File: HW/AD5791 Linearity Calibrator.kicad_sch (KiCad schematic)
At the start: 56 parts, among them J1 OUTPUT, J10 Conn_01x01, J2 PWR, J3 REF, J4 REF, J5 REF, J6 REF, J7 Conn_01x01, J8 Conn_01x01, J9 Conn_01x01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

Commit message: Layout Rev 2 Finished?
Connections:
- net UART_RX: now reaches U12.6 (VOB)
- net UART_RX: now also U1.2 (GPIO1)
- net UART_TX: now reaches U12.7 (VIA)
- net UART_TX: now also U1.1 (GPIO0)
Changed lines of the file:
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@@
+    (stroke (width 0) (type default))
+  )
+  (wire (pts (xy 231.14 173.99) (xy 240.03 173.99))
     (stroke (width 0) (type default))
   )
@@
   )
   (wire (pts (xy 217.17 255.27) (xy 207.01 255.27))
+    (stroke (width 0) (type default))
+  )
+  (wire (pts (xy 231.14 179.07) (xy 240.03 179.07))
     (stroke (width 0) (type default))
   )
@@
     (effects (font (size 1.27 1.27)) (justify right bottom))
   )
+  (label "UART_RX" (at 316.23 167.64 0) (fields_autoplaced)
+    (effects (font (size 1.27 1.27)) (justify left bottom))
+  )
   (label "~{LDAC}" (at 226.06 92.71 0) (fields_autoplaced)
     (effects (font (size 1.27 1.27)) (justify left bottom))
@@
     (effects (font (size 1.27 1.27)) (justify left bottom))
   )
+  (label "UART_TX" (at 240.03 173.99 180) (fields_autoplaced)
+    (effects (font (size 1.27 1.27)) (justify right bottom))
+  )
   (label "REF" (at 74.93 129.54 180) (fields_autoplaced)
     (effects (font (size 1.27 1.27)) (justify right bottom))
@@
     (effects (font (size 1.27 1.27)) (justify left bottom))
   )
+  (label "UART_RX" (at 240.03 179.07 180) (fields_autoplaced)
+    (effects (font (size 1.27 1.27)) (justify right bottom))
+  )
+  (label "UART_TX" (at 316.23 165.1 0) (fields_autoplaced)
+    (effects (font (size 1.27 1.27)) (justify left bottom))
+  )

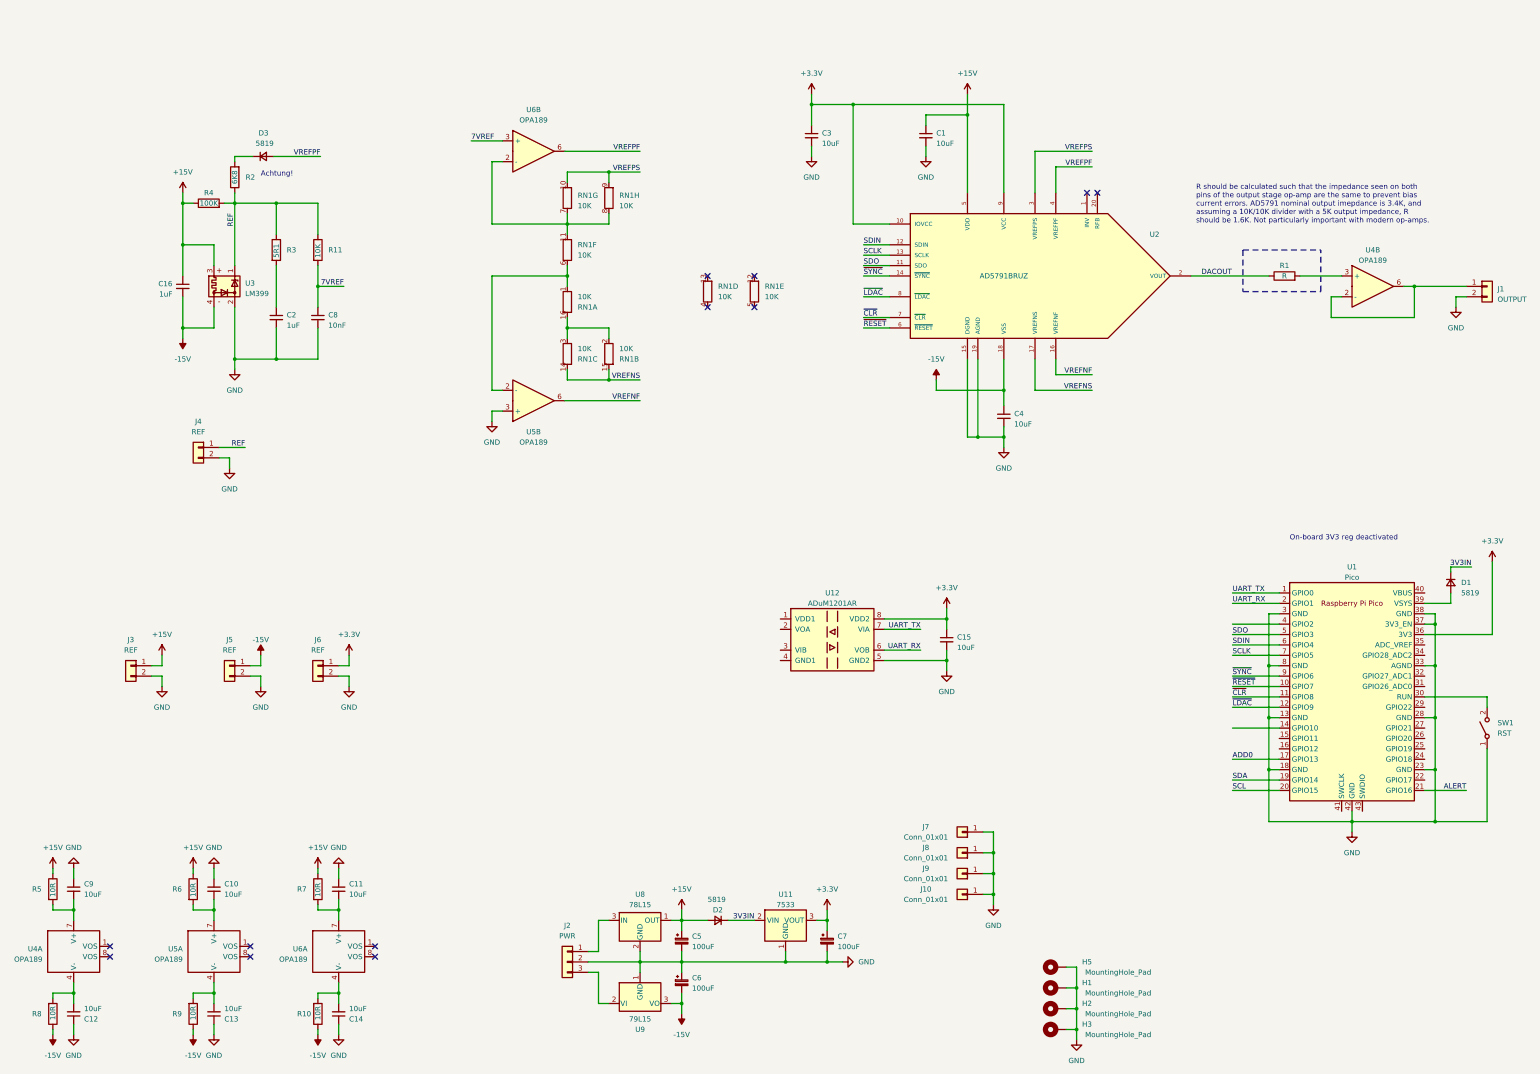
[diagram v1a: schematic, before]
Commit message: 4 wire buffer, keepout under isolator traces
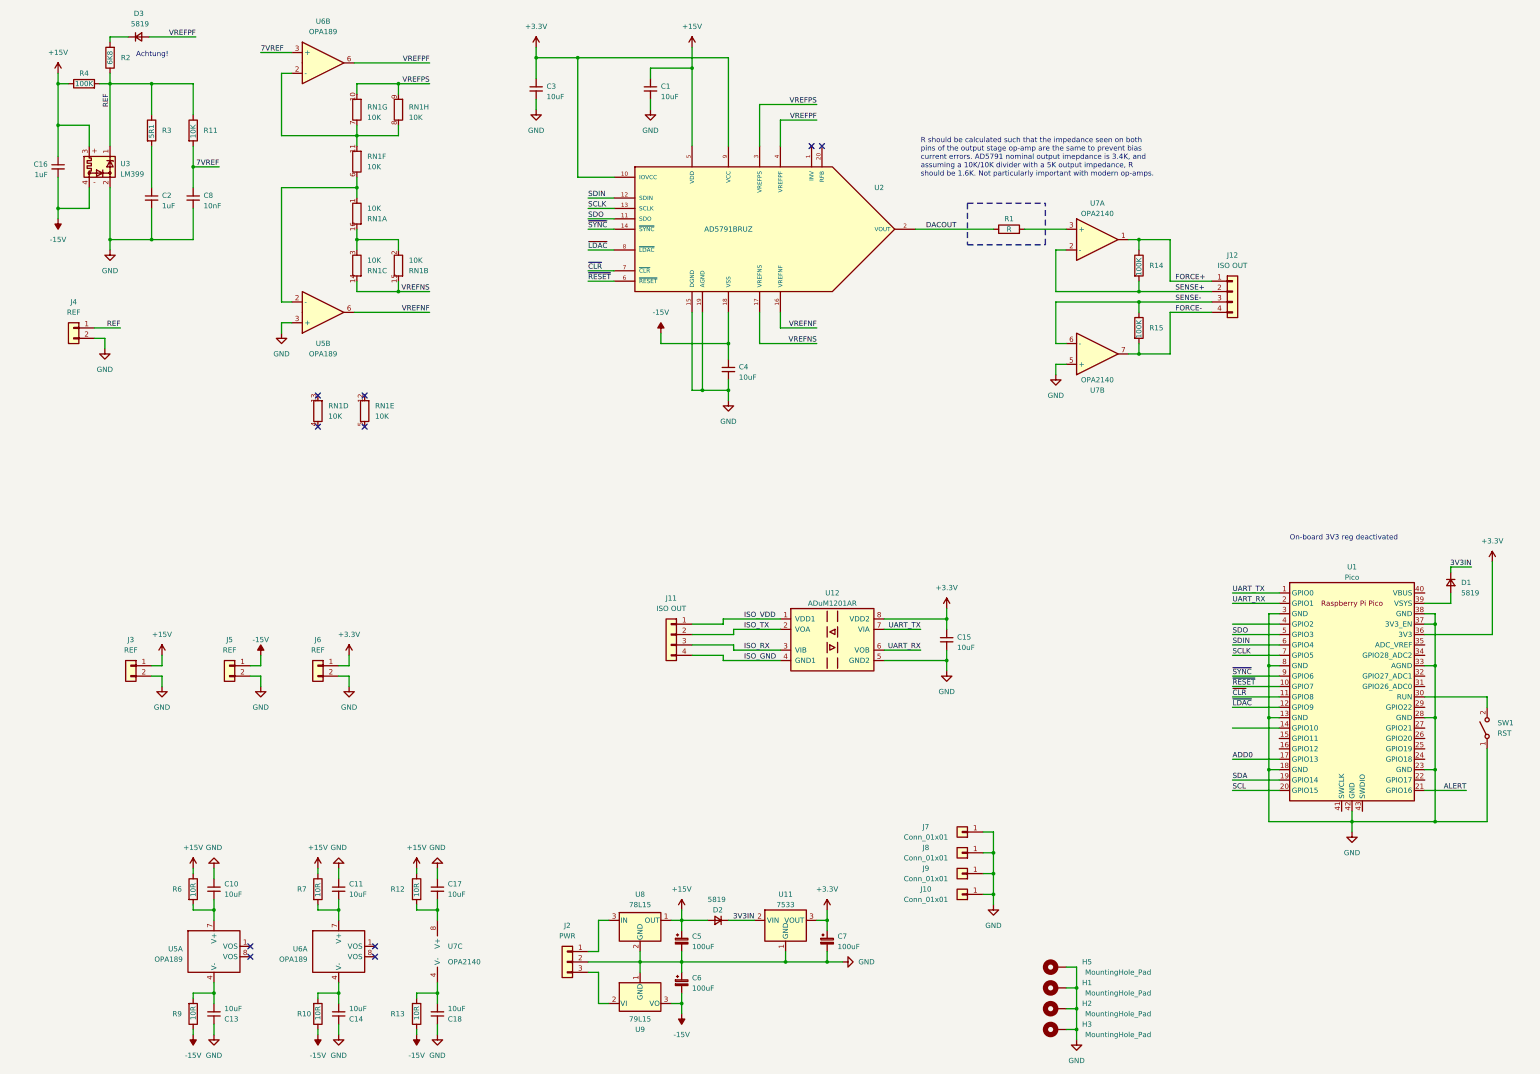
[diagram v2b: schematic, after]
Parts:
- removed C12, C9: 10uF, Resistor_SMD:R_0603_1608Metric, symbol Device:C_Small
- removed J1: OUTPUT, Connector_PinHeader_2.54mm:PinHeader_1x02_P2.54mm_Vertical, symbol Connector_Generic:Conn_01x02
- removed R5, R8: 10R, Resistor_SMD:R_0603_1608Metric, symbol Device:R
- removed U4: OPA189, Package_SO:SOIC-8_3.9x4.9mm_P1.27mm, symbol Better Op-Amp:Better_Op-Amp
- added C17, C18: 10uF, Resistor_SMD:R_0603_1608Metric, symbol Device:C_Small
- added J11, J12: ISO OUT, Connector_PinHeader_2.54mm:PinHeader_1x04_P2.54mm_Vertical, symbol Connector_Generic:Conn_01x04
- added R12, R13: 10R, Resistor_SMD:R_0603_1608Metric, symbol Device:R
- added R14, R15: 100K, Resistor_SMD:R_0603_1608Metric, symbol Device:R
- added U7: OPA2140, Package_SO:SOIC-8_3.9x4.9mm_P1.27mm, symbol Device:Opamp_Dual
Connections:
- net +15V: now also R12.1
- net -15V: now also R13.1
- net GND: now also C17.1, C18.1, U7.5 (+)
- net at R1.2: now also U7.3 (+)
- net ISO_VDD: now reaches U12.1 (VDD1)
- net ISO_VDD: now also J11.1 (Pin_1)
- net ISO_TX: now reaches U12.2 (VOA)
- net ISO_TX: now also J11.2 (Pin_2)
- net ISO_RX: now reaches U12.3 (VIB)
- net ISO_RX: now also J11.3 (Pin_3)
- net ISO_GND: now reaches U12.4 (GND1)
- net ISO_GND: now also J11.4 (Pin_4)
- new net: C17.2, R12.2, U7.8 (V+)
- new net: C18.2, R13.2, U7.4 (V-)
- new net FORCE+: J12.1 (Pin_1), R14.1, U7.1
- new net FORCE-: J12.4 (Pin_4), R15.2, U7.7
- new net SENSE+: J12.2 (Pin_2), R14.2, U7.2 (-)
- new net SENSE-: J12.3 (Pin_3), R15.1, U7.6 (-)
- no-connect marks 12 -> 10
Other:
- moved on the sheet: C1, C16, C2, C3, C4, C8, D3, J4, R1, R11, R2, R3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

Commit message: Layout Rev 3
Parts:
- added C9: 10uF, Resistor_SMD:R_0603_1608Metric, symbol Device:C_Small
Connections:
- net ISO_GND: now also C9.2
- net ISO_VDD: now also C9.1
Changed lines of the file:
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@@
+    (stroke (width 0) (type default))
+  )
+  (wire (pts (xy 260.35 170.18) (xy 260.35 173.99))
     (stroke (width 0) (type default))
   )
@@
     (stroke (width 0) (type default))
   )
+  (wire (pts (xy 260.35 179.07) (xy 260.35 184.15))
+    (stroke (width 0) (type default))
+  )
   (wire (pts (xy 62.23 264.16) (xy 62.23 262.89))
     (stroke (width 0) (type default))
@@
     (effects (font (size 1.27 1.27)) (justify left bottom))
   )
+  (label "ISO_GND" (at 260.35 184.15 0) (fields_autoplaced)
+    (effects (font (size 1.27 1.27)) (justify left bottom))
+  )
   (label "SDA" (at 316.23 210.82 0) (fields_autoplaced)
     (effects (font (size 1.27 1.27)) (justify left bottom))
   )
   (label "ISO_GND" (at 196.85 181.61 0) (fields_autoplaced)
+    (effects (font (size 1.27 1.27)) (justify left bottom))
+  )
+  (label "ISO_VDD" (at 260.35 170.18 0) (fields_autoplaced)
     (effects (font (size 1.27 1.27)) (justify left bottom))
   )
@@
         )
       )
+    )
+  )
+  (symbol (lib_id "Device:C_Small") (at 260.35 176.53 0) (unit 1)
+    (in_bom yes) (on_board yes) (dnp no) (fields_autoplaced)
+    (property "Reference" "C9" (at 262.89 175.9013 0)
+      (effects (font (size 1.27 1.27)) (justify left))
+    )
+    (property "Value" "10uF" (at 262.89 178.4413 0)
+      (effects (font (size 1.27 1.27)) (justify left))
+    )
+    (property "Footprint" "Resistor_SMD:R_0603_1608Metric" (at 260.35 176.53 0)
+      (effects (font (size 1.27 1.27)) hide)
+    )
+    (property "Datasheet" "~" (at 260.35 176.53 0)
+      (effects (font (size 1.27 1.27)) hide)
+    )
+    (pin "1")
+    (pin "2")
+    (instances
+      (project "AD5791 Linearity Calibrator"
+        (path "/545249ea-2c8e-4b30-8f2b-5f4518163292"
+          (reference "C9") (unit 1)
+        )
+      )

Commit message: star ground added
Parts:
- added JP1: GND BRIDGE, 0603 Jumper:0603 Jumper, symbol Jumper:SolderJumper_2_Open
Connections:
- net GND: now also JP1.1 (A); no longer C2.2, C8.2, U2.19 (AGND), U3.2, U5.3 (+), U7.5 (+)
- new net GNDA: C2.2, C8.2, JP1.2 (B), U2.19 (AGND), U3.2, U5.3 (+), U7.5 (+)

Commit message: Layout Rev 4
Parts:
- added D4: 5819, Resistor_SMD:R_0603_1608Metric_Pad0.98x0.95mm_HandSolder, symbol Device:D_Small
- R11: footprint Resistor_SMD:R_0603_1608Metric -> 0603 Jumper:0603 Jumper
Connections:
- net +15V: now also D4.1 (K)
- net +3.3V: now also D4.2 (A)
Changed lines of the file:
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@@
   (junction (at 146.05 34.29) (diameter 0) (color 0 0 0 0)
   )
+  (junction (at 193.04 53.34) (diameter 0) (color 0 0 0 0)
+  )
   (junction (at 193.04 115.57) (diameter 0) (color 0 0 0 0)
   )
@@
   (junction (at 278.13 266.7) (diameter 0) (color 0 0 0 0)
   )
+  (junction (at 184.15 53.34) (diameter 0) (color 0 0 0 0)
+  )
   (junction (at 246.38 171.45) (diameter 0) (color 0 0 0 0)
   )
@@
     (stroke (width 0) (type default))
   )
-  (wire (pts (xy 184.15 55.88) (xy 184.15 36.83))
+  (wire (pts (xy 184.15 55.88) (xy 184.15 53.34))
     (stroke (width 0) (type default))
   )
@@
     (stroke (width 0) (type default))
   )
+  (wire (pts (xy 184.15 53.34) (xy 184.15 36.83))
+    (stroke (width 0) (type default))
+  )
   (wire (pts (xy 293.37 88.9) (xy 293.37 91.44))
     (stroke (width 0) (type default))
@@
     (stroke (width 0) (type default))
   )
-  (wire (pts (xy 193.04 34.29) (xy 193.04 55.88))
+  (wire (pts (xy 193.04 34.29) (xy 193.04 53.34))
     (stroke (width 0) (type default))
   )
@@
     (stroke (width 0) (type default))
   )
+  (wire (pts (xy 190.5 53.34) (xy 193.04 53.34))
+    (stroke (width 0) (type default))
+  )
   (wire (pts (xy 316.23 205.74) (xy 327.66 205.74))
     (stroke (width 0) (type default))
@@
     (stroke (width 0) (type default))
   )
+  (wire (pts (xy 193.04 53.34) (xy 193.04 55.88))
+    (stroke (width 0) (type default))
+  )
   (wire (pts (xy 327.66 182.88) (xy 325.12 182.88))
     (stroke (width 0) (type default))
@@
     (stroke (width 0) (type default))
   )
+  (wire (pts (xy 184.15 53.34) (xy 185.42 53.34))
+    (stroke (width 0) (type default))
+  )
   (wire (pts (xy 365.76 170.18) (xy 365.76 172.72))
     (stroke (width 0) (type default))
@@
     )
   )
+  (symbol (lib_id "Device:D_Small") (at 187.96 53.34 0) (unit 1)
+    (in_bom yes) (on_board yes) (dnp no)
+    (property "Reference" "D4" (at 189.23 49.53 0)
+      (effects (font (size 1.27 1.27)) (justify right))
+    )
+    (property "Value" "5819" (at 190.5 46.99 0)
+      (effects (font (size 1.27 1.27)) (justify right))
+    )
+    (property "Footprint" "Resistor_SMD:R_0603_1608Metric_Pad0.98x0.95mm_HandSolder" (at 187.96 53.34 90)
+      (effects (font (size 1.27 1.27)) hide)
+    )
+    (property "Datasheet" "~" (at 187.96 53.34 90)
+      (effects (font (size 1.27 1.27)) hide)
+    )
+    (property "Sim.Device" "D" (at 187.96 53.34 0)
+      (effects (font (size 1.27 1.27)) hide)
+    )
+    (property "Sim.Pins" "1=K 2=A" (at 187.96 53.34 0)
+      (effects (font (size 1.27 1.27)) hide)
+    )
+    (pin "1")
+    (pin "2")
+    (instances
+      (project "AD5791 Linearity Calibrator"
+        (path "/545249ea-2c8e-4b30-8f2b-5f4518163292"
+          (reference "D4") (unit 1)
+        )
+      )
+    )
+  )
   (symbol (lib_id "power:GNDA") (at 186.69 118.11 0) (unit 1)
     (in_bom yes) (on_board yes) (dnp no) (fields_autoplaced)
@@
       (effects (font (size 1.27 1.27)) (justify left))
     )
-    (property "Footprint" "Resistor_SMD:R_0603_1608Metric" (at 60.452 52.07 90)
+    (property "Footprint" "0603 Jumper:0603 Jumper" (at 60.452 52.07 90)
       (effects (font (size 1.27 1.27)) hide)
     )
